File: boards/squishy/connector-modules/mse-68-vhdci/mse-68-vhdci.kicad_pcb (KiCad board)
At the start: 6 copper layers, 75 x 55 mm, 18 parts, among them J1 SCSI PHY Mezz, J2 Conn_02x25_Odd_Even, J3 Conn_01x04, U1 M24C02-RMC

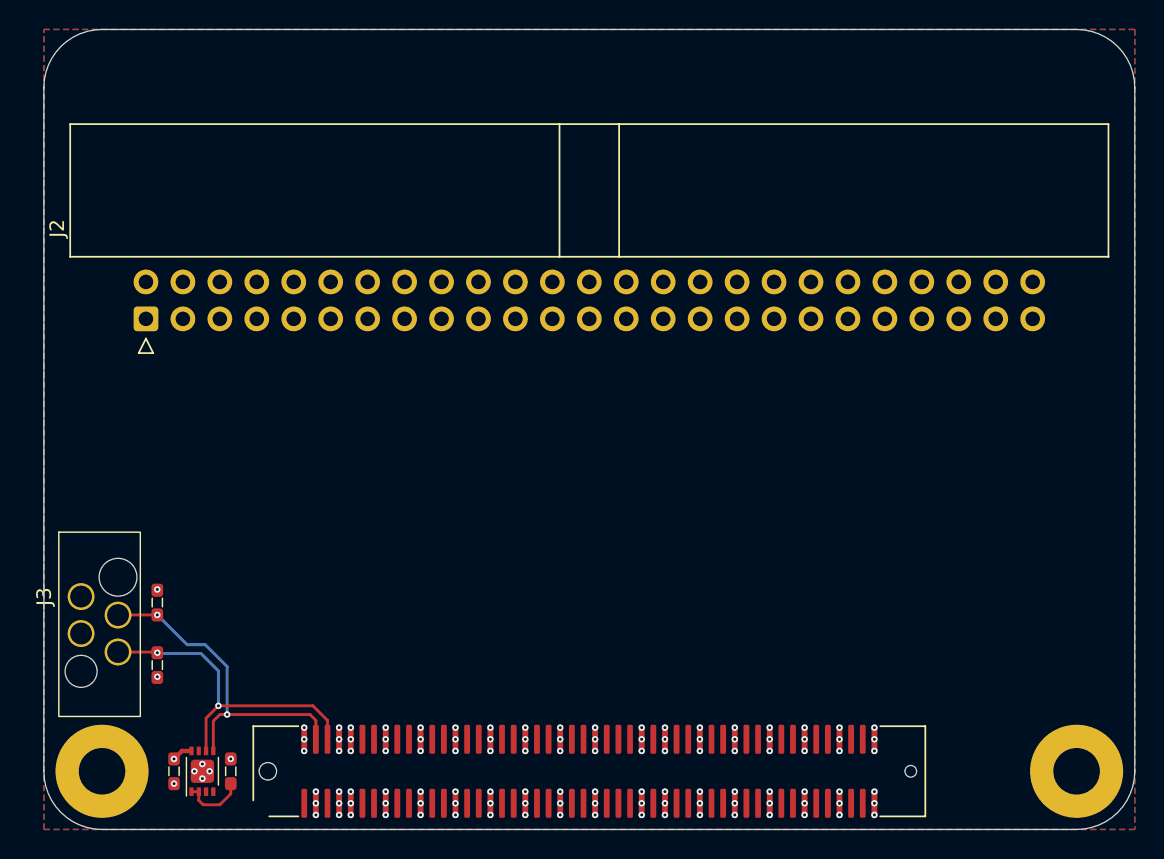
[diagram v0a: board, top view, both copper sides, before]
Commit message: squishy: connectors: Propagated changes from mse-68-hd PCB and DRC rules to mse-68-vhdci
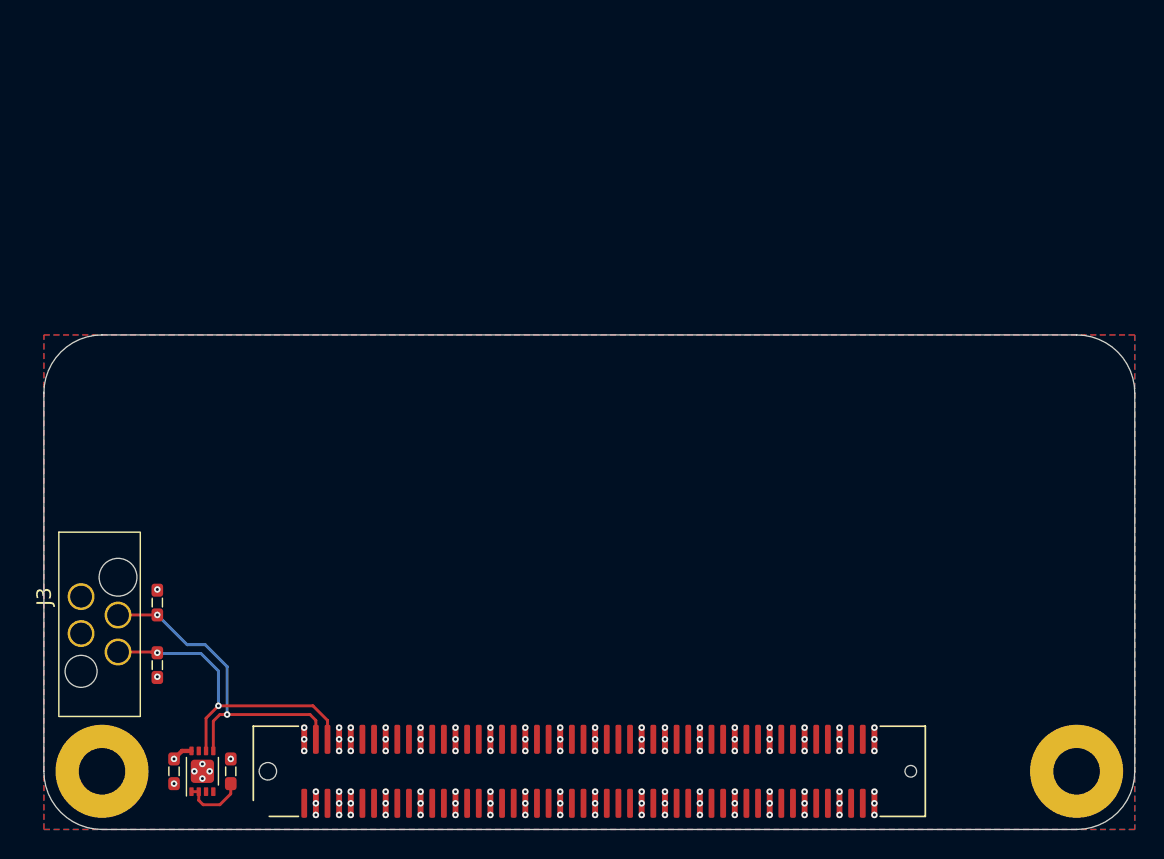
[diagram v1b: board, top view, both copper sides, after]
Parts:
- removed J2: Conn_02x25_Odd_Even, Connector_IDC:IDC-Header_2x25_P2.54mm_Horizontal
- moved REF** 21.0 mm to (121.0, 105.8)
- moved REF** 21.0 mm to (174.0, 105.8)
- moved REF** 16.2 mm to (109.7, 115.0)
- moved REF** 16.2 mm to (185.2, 115.0)
- moved REF** 4.75 mm to (185.2, 131.0)
- moved REF** 4.75 mm to (109.7, 131.0)
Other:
- board size 75 x 55 mm -> 75 x 34 mm
- board text added: "0.2028mm"
- board text added: "0.2104mm"
- board text added: "0.4000mm"
- board text added: "IFF JLCPCB: JLC06161H-7628"
- board text added: "Impedance Table: 50Ω Coplanar Single Ended (inner): width: TODO 72Ω Coplanar Single Ended (outter): width: 0.1115mm 72Ω Non-Coplanar Single Ended (outter): width: 0.1514mm 50Ω Non-Coplanar Single Ended (inner): width: TODO 120Ω Coplanar Differential (outter): width: 0.1148, space: 0.2mm 120Ω Non-Coplanar Differential (outter): width: 0.1275, space: 0.2mm"
- board text added: "Outter Copper: 1oz Inner Copper: 0.5oz"
- board text added: "Prepreg (7628*1)"
- board text removed: "0.0994mm"
- board text removed: "0.1088mm"
- board text removed: "0.5500mm"
- board text removed: "IFF JLCPCB: JLC06161H-3313"
- board text removed: "Impedance Table: 50Ω Coplanar Signle Ended (inner): width: TODO 50Ω Coplanar Signle Ended (outter): width: TODO 50Ω Non-Coplanar Signle Ended (inner): width: TODO 50Ω Non-Coplanar Signle Ended (outter): width: TODO"
- board text removed: "Outter Copper: 1Oz Inner Copper: 0.5Oz"
- board text removed: "Prepreg (2116*1)"
- board text removed: "Prepreg (3313*1)"

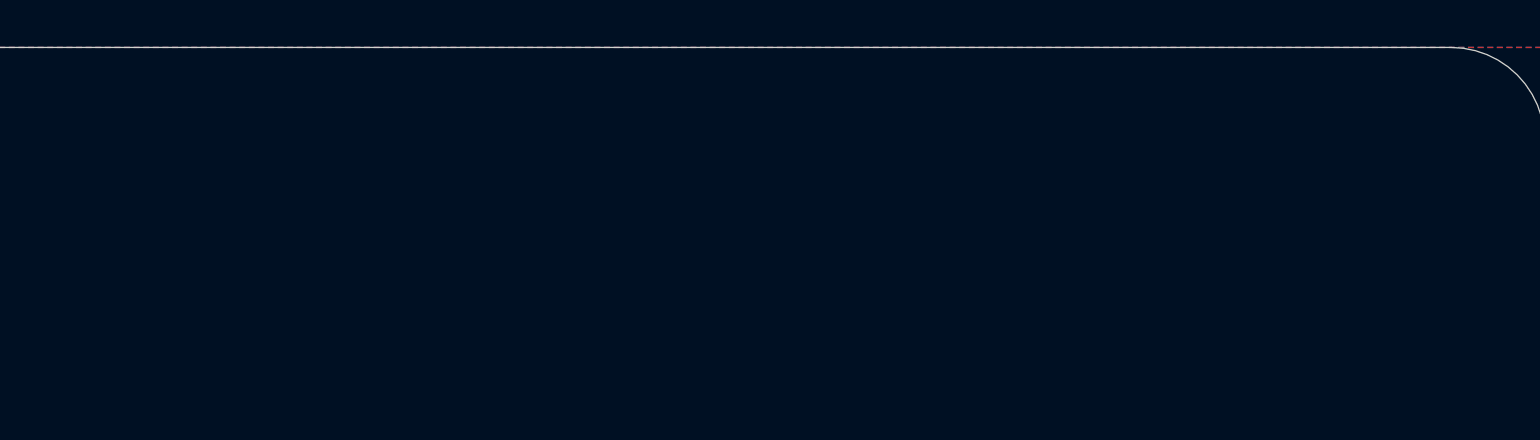
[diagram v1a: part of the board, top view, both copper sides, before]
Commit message: squishy: connectors: hooked up mse-68-vhdci connector
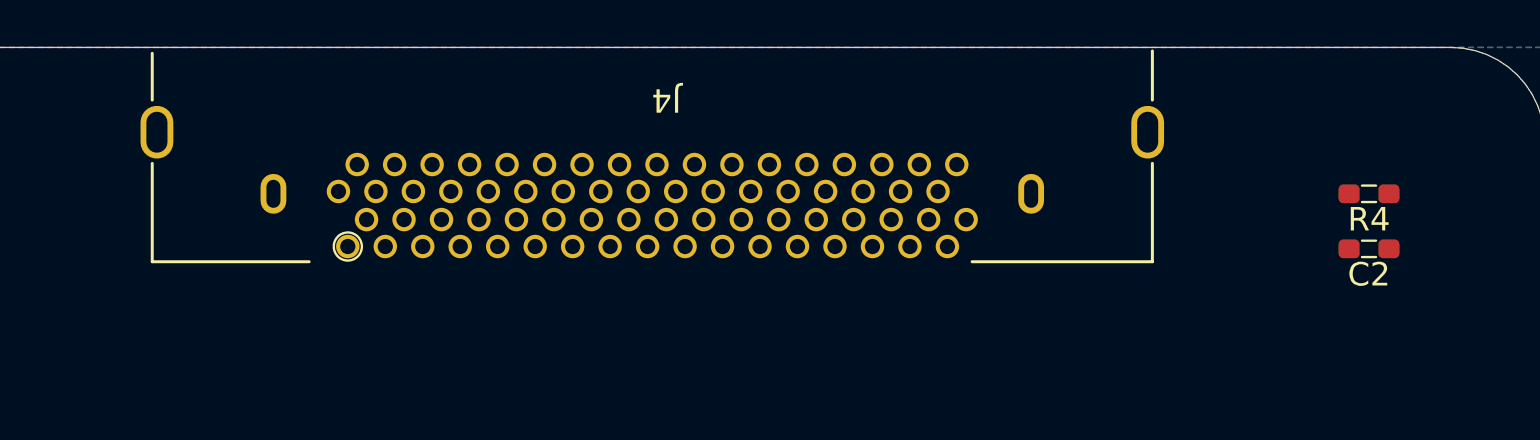
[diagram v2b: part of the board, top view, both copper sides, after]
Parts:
- added C2: 100n, rhais_rcl:C0603, F.Cu at (177.5, 114.6)
- added J4: VHDCI, lethalbit-connectors:5796055, F.Cu at (147.5, 112.7)
- added R4: 1M, rhais_rcl:R0603, F.Cu at (177.5, 112.2)

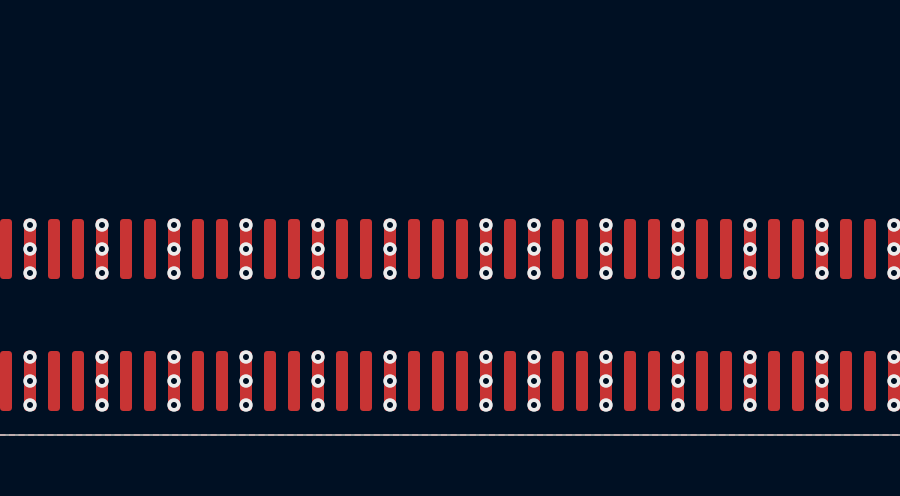
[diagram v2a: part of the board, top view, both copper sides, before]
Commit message: squishy: connectors: Fixed the pour layers and added TERMPWR stitching for mse-68-vhdci
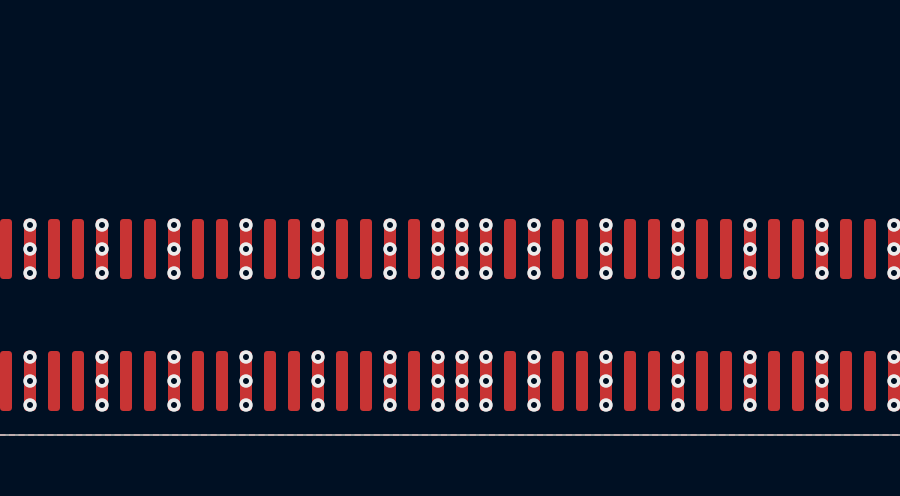
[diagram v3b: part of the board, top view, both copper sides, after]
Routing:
- net /CON.TERMPWR: vias 0 -> 12
- added copper zone on In2.Cu, net +3V3
- added copper zone on In2.Cu, net /CON.TERMPWR
- removed copper zone on In1.Cu, net +3V3
- removed copper zone on In2.Cu, net GND
